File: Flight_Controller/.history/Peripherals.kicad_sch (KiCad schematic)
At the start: 44 parts, among them IC1 AT7456E, U2 BMI270, U3 TLV75533PDBV, U4 W25Q128JVSIQ TR, U5 TPS62932, Y2 ABM3-27.000MHZ-D2Y-T

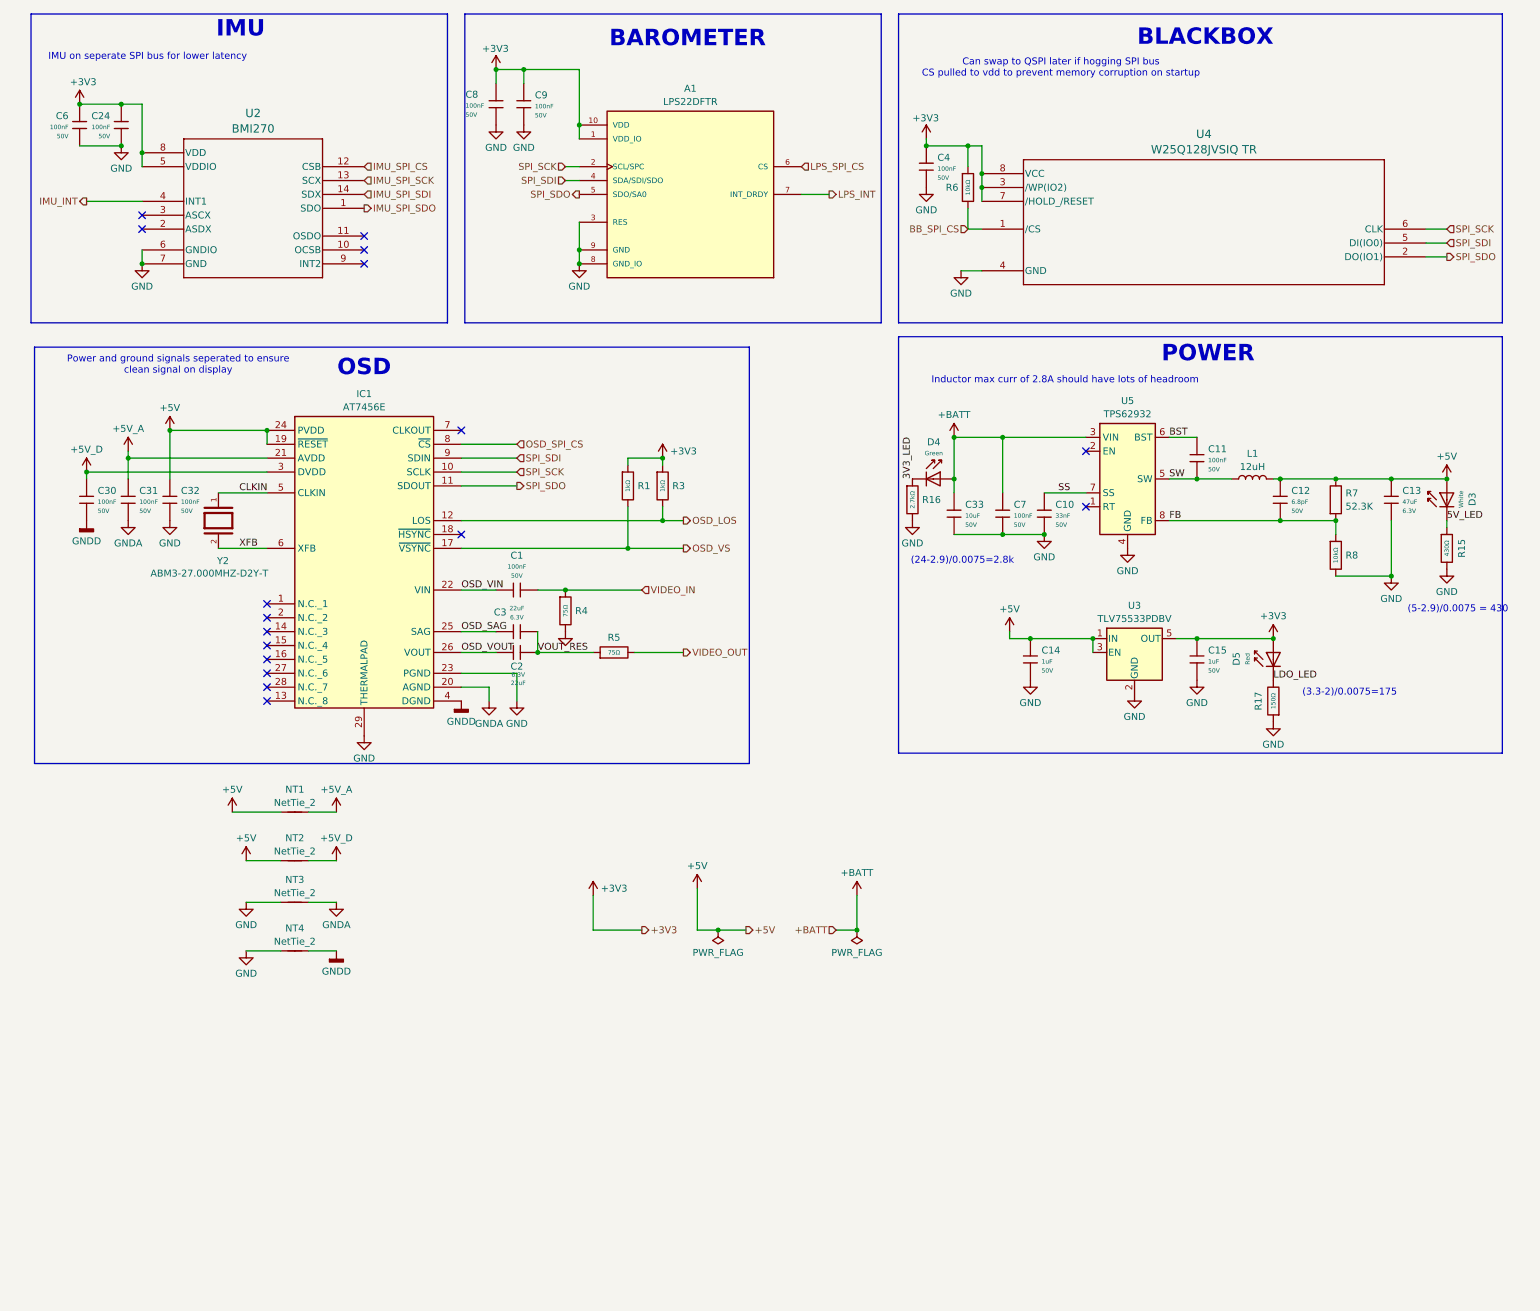
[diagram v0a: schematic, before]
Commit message: Updated buck for 60v spike
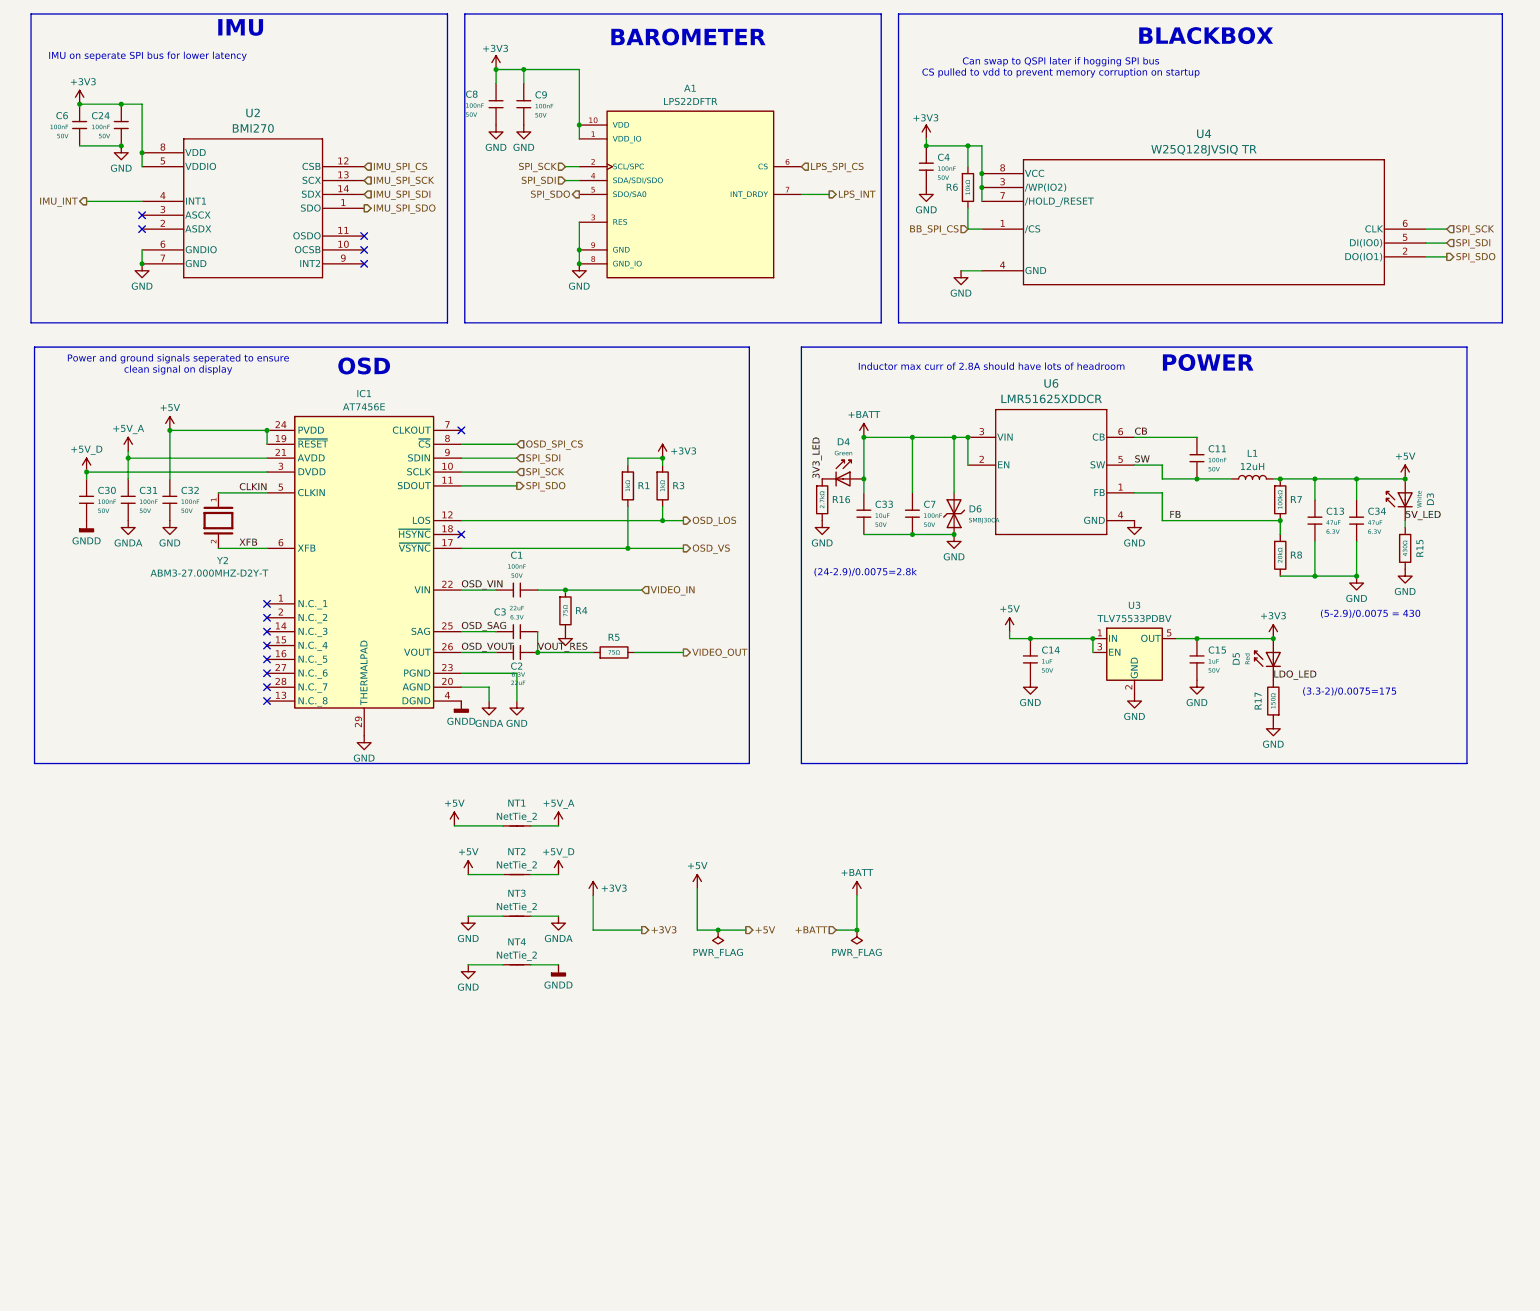
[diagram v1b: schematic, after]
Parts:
- removed C10: 33nF, PCM_JLCPCB:C_0603, symbol PCM_JLCPCB-Capacitors:0603,33nF
- removed C12: 6.8pF, PCM_JLCPCB:C_0603, symbol PCM_JLCPCB-Capacitors:0603,6.8pF
- removed R7: 52.3K, PCM_JLCPCB:R_0603, symbol Device:R
- removed R8: 10kΩ, PCM_JLCPCB:R_0603, symbol PCM_JLCPCB-Resistors:0603,10kΩ
- removed U5: TPS62932, Package_TO_SOT_SMD:SOT-583-8, symbol Regulator_Switching:TPS62932
- added C34: 47uF, PCM_JLCPCB:C_0805, symbol PCM_JLCPCB-Capacitors:0805,47uF
- added D6: SMBJ30CA, PCM_JLCPCB:D_SMB, symbol PCM_JLCPCB-Diodes:TVS-Bi,SMBJ30CA
- added R7: 100kΩ, PCM_JLCPCB:R_0603, symbol PCM_JLCPCB-Resistors:0603,100kΩ
- added R8: 20kΩ, PCM_JLCPCB:R_0603, symbol PCM_JLCPCB-Resistors:0603,20kΩ
- added U6: LMR51625XDDCR, Flight_Controller:DDC0006A-MFG, symbol Flight_Controller:LMR51625XDDCR
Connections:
- net +5V: now also C34.1, R7.1
- net +BATT: now also D6.2, U6.2 (EN), U6.3 (VIN)
- net FB: now also R7.2, R8.1, U6.1 (FB)
- net GND: now also C34.2, D6.1, R8.2, U6.4 (GND)
- net SW: now also U6.5 (SW)
- net BST renamed CB
- net CB: now also U6.6 (CB)
- no-connect marks 17 -> 15
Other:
- moved on the sheet: C13, C33, C7, D3, D4, NT1, NT2, NT3, NT4, R15, R16

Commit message: Initial Layout Done
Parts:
- NT1, NT2, NT3, NT4: footprint NetTie:NetTie-2_THT_Pad1.0mm -> NetTie:NetTie-2_SMD_Pad0.5mm
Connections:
- net 3V3_LED renamed BATT_LED
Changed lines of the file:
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@@
 		)
 	)
-	(label "3V3_LED"
+	(label "BATT_LED"
 		(at 158.75 102.87 90)
 		(effects
@@
 			)
 		)
-		(property "Footprint" "NetTie:NetTie-2_THT_Pad1.0mm"
+		(property "Footprint" "NetTie:NetTie-2_SMD_Pad0.5mm"
 			(at 102.87 175.26 0)
 			(hide yes)
@@
 			)
 		)
-		(property "Footprint" "NetTie:NetTie-2_THT_Pad1.0mm"
+		(property "Footprint" "NetTie:NetTie-2_SMD_Pad0.5mm"
 			(at 102.87 191.77 0)
 			(hide yes)
@@
 			)
 		)
-		(property "Footprint" "NetTie:NetTie-2_THT_Pad1.0mm"
+		(property "Footprint" "NetTie:NetTie-2_SMD_Pad0.5mm"
 			(at 102.87 182.88 0)
 			(hide yes)
@@
 			)
 		)
-		(property "Footprint" "NetTie:NetTie-2_THT_Pad1.0mm"
+		(property "Footprint" "NetTie:NetTie-2_SMD_Pad0.5mm"
 			(at 102.87 166.37 0)
 			(hide yes)

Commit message: Updated Connector Standard
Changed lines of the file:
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@@
 	(rectangle
 		(start 154.94 78.74)
-		(end 276.733 154.94)
+		(end 276.733 165.735)
 		(stroke
 			(width 0)

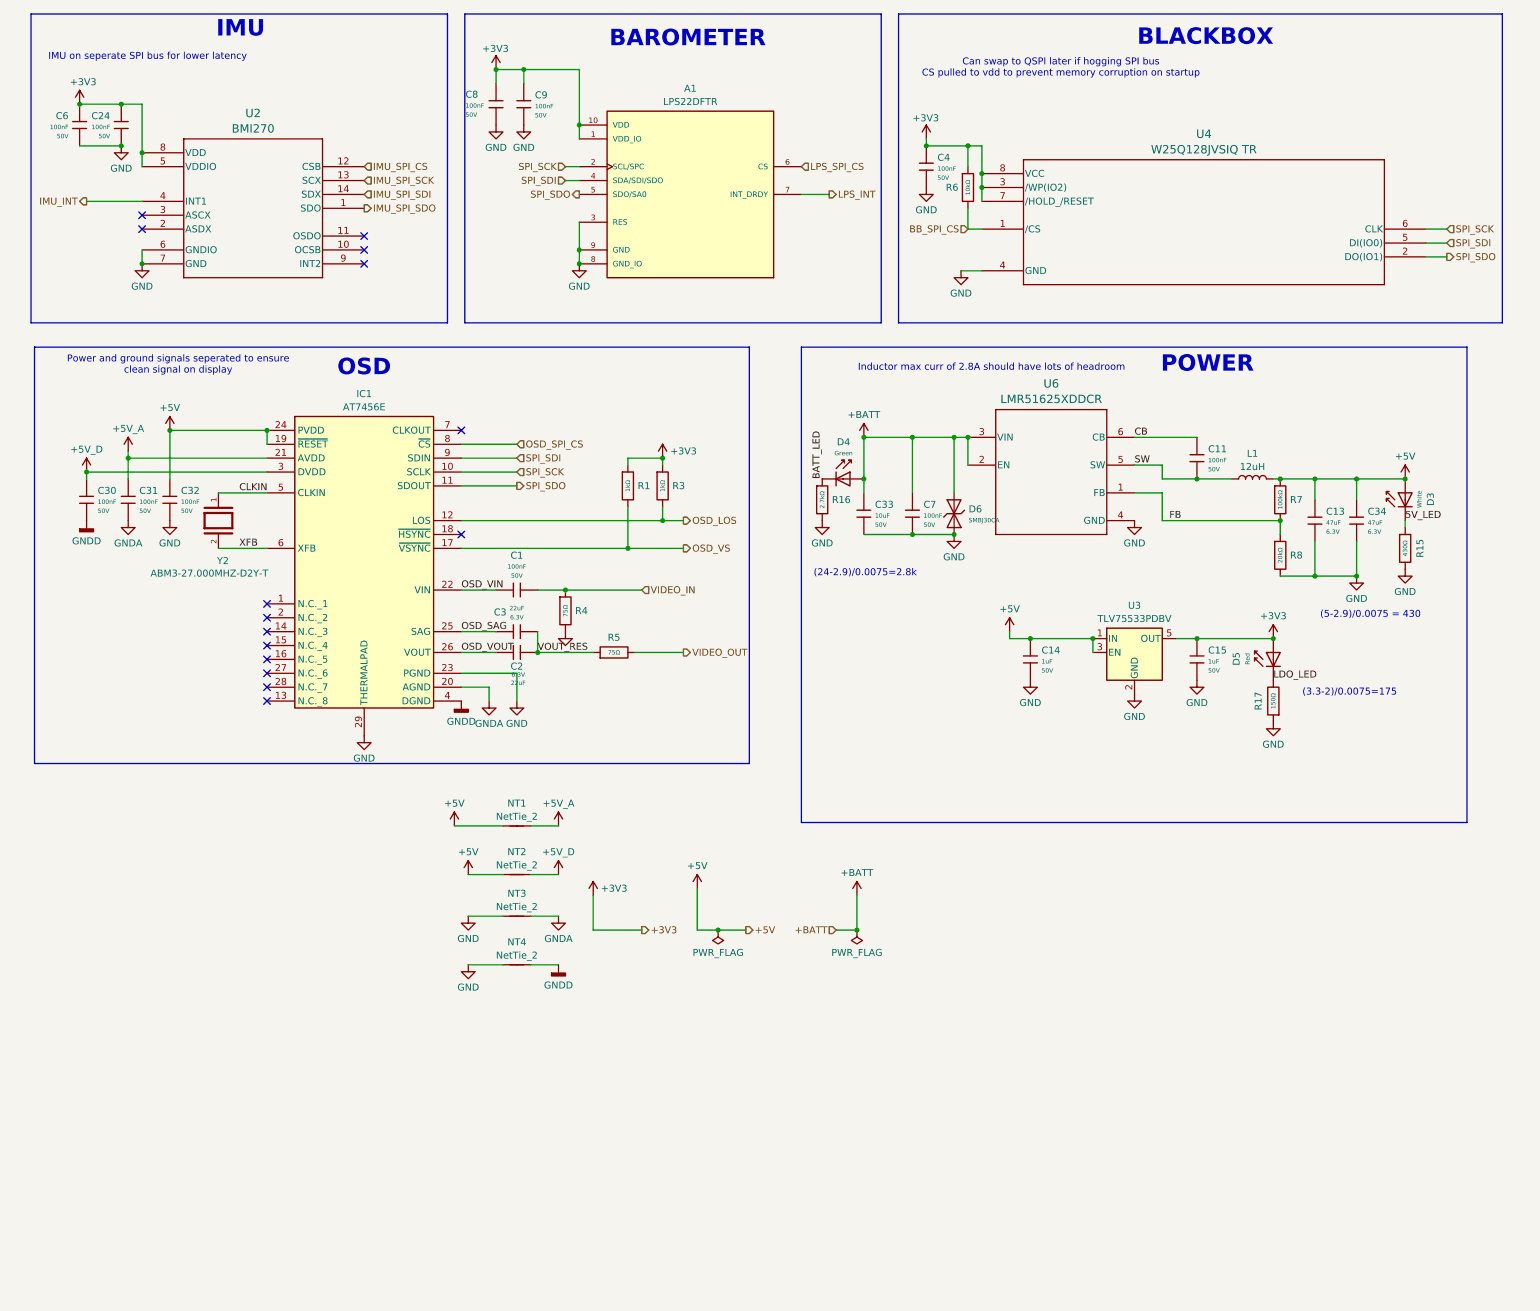
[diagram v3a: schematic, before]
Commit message: Added 9V Buck, GPS + Mag, Digital VTX
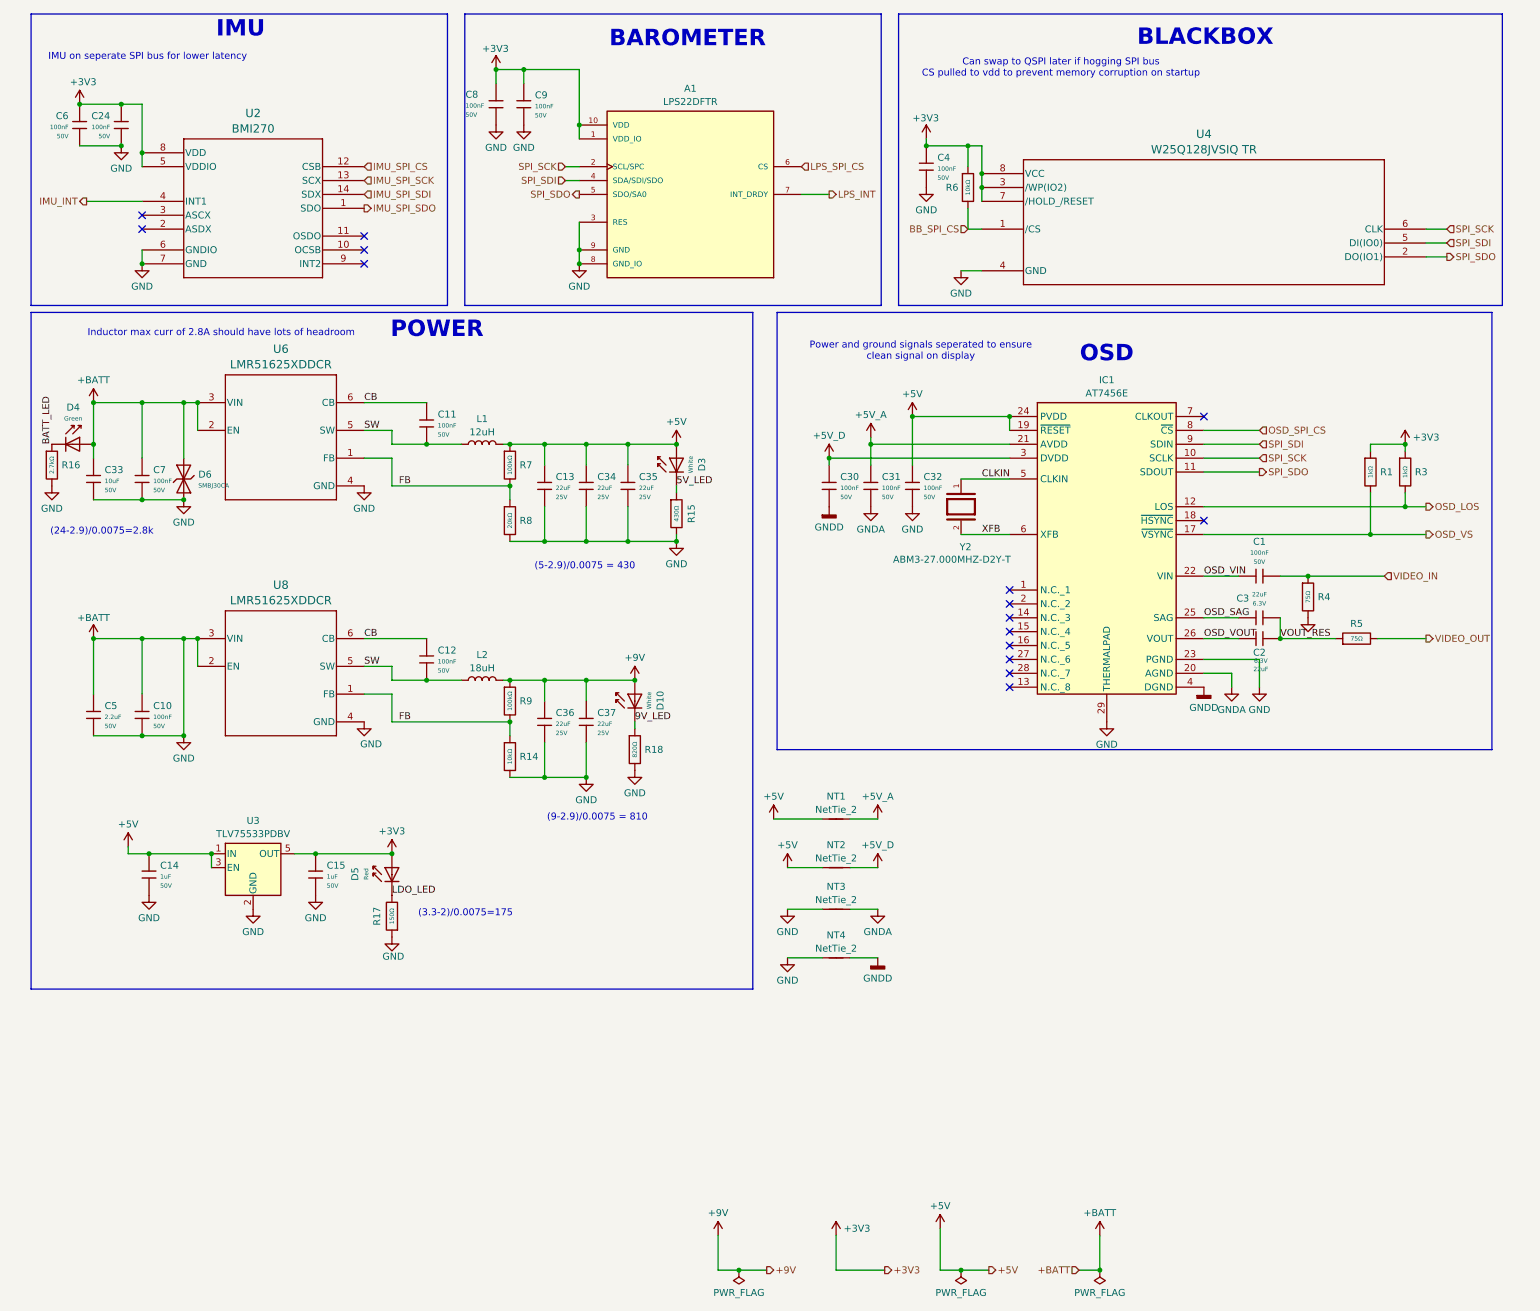
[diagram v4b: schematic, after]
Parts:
- removed C13, C34: 47uF, PCM_JLCPCB:C_0805, symbol PCM_JLCPCB-Capacitors:0805,47uF
- added C10, C12: 100nF, PCM_JLCPCB:C_0603, symbol PCM_JLCPCB-Capacitors:0603,100nF
- added C13, C34, C35, C36, C37: 22uF, PCM_JLCPCB:C_1206, symbol PCM_JLCPCB-Capacitors:1206,22uF,(2)
- added C5: 2.2uF, PCM_JLCPCB:C_0805, symbol PCM_JLCPCB-Capacitors:0805,2.2uF
- added D10: White, PCM_JLCPCB:D_0603, symbol PCM_JLCPCB-Diodes:LED,0603,White
- added L2: 18uH, Inductor_SMD:L_TDK_VLS6045EX_VLS6045AF, symbol Device:L
- added R14: 10kΩ, PCM_JLCPCB:R_0603, symbol PCM_JLCPCB-Resistors:0603,10kΩ
- added R18: 820Ω, PCM_JLCPCB:R_0603, symbol PCM_JLCPCB-Resistors:0603,820Ω
- added R9: 100kΩ, PCM_JLCPCB:R_0603, symbol PCM_JLCPCB-Resistors:0603,100kΩ
- added U8: LMR51625XDDCR, Flight_Controller:DDC0006A-MFG, symbol Flight_Controller:LMR51625XDDCR
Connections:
- net GND is gone; now on net +BATT: A1.3 (RES), A1.8 (GND_IO), A1.9 (GND), C14.2, C15.2, C24.2, C32.2, C33.2, C4.2, C6.2, C7.2, C8.2, C9.2, D6.1, IC1.23 (PGND), IC1.29 (THERMALPAD), NT3.2, NT4.2, R15.2, R16.2, R17.1, R4.2, R8.2, U2.6 (GNDIO), U2.7 (GND), U3.2 (GND), U4.4 (GND), U6.4 (GND)
- net +5V: now also C13.1, C34.1, C35.1
- net +BATT: now also C10.1, C10.2, C13.2, C34.2, C35.2, C36.2, C37.2, C5.1, C5.2, R14.2, R18.2, U8.2 (EN), U8.3 (VIN), U8.4 (GND)
- net CB: now also C12.1, U8.6 (CB)
- net FB: now also R14.1, R9.2, U8.1 (FB)
- net SW: now also C12.2, L2.1, U8.5 (SW)
- new net +9V: C36.1, C37.1, D10.2, L2.2, R9.1
- new net 9V_LED: D10.1, R18.1
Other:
- note added: "(9-2.9)/0.0075 = 810"
- moved on the sheet: C1, C11, C14, C15, C2, C3, C30, C31, C32, C33, C7, D3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
